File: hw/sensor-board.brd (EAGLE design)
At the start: 50 x 40 mm, 55 parts, among them U1 LT1762EMS8-3.3PBF, U2 ULN2003LVPWR, U3 ULN2003LVPWR, U4 PCA9685PW, U5 AT42QT1070-SSU, U6 TPS730XX, X1 MOLEX-501953-0407, X2 MOLEX-501953-0407

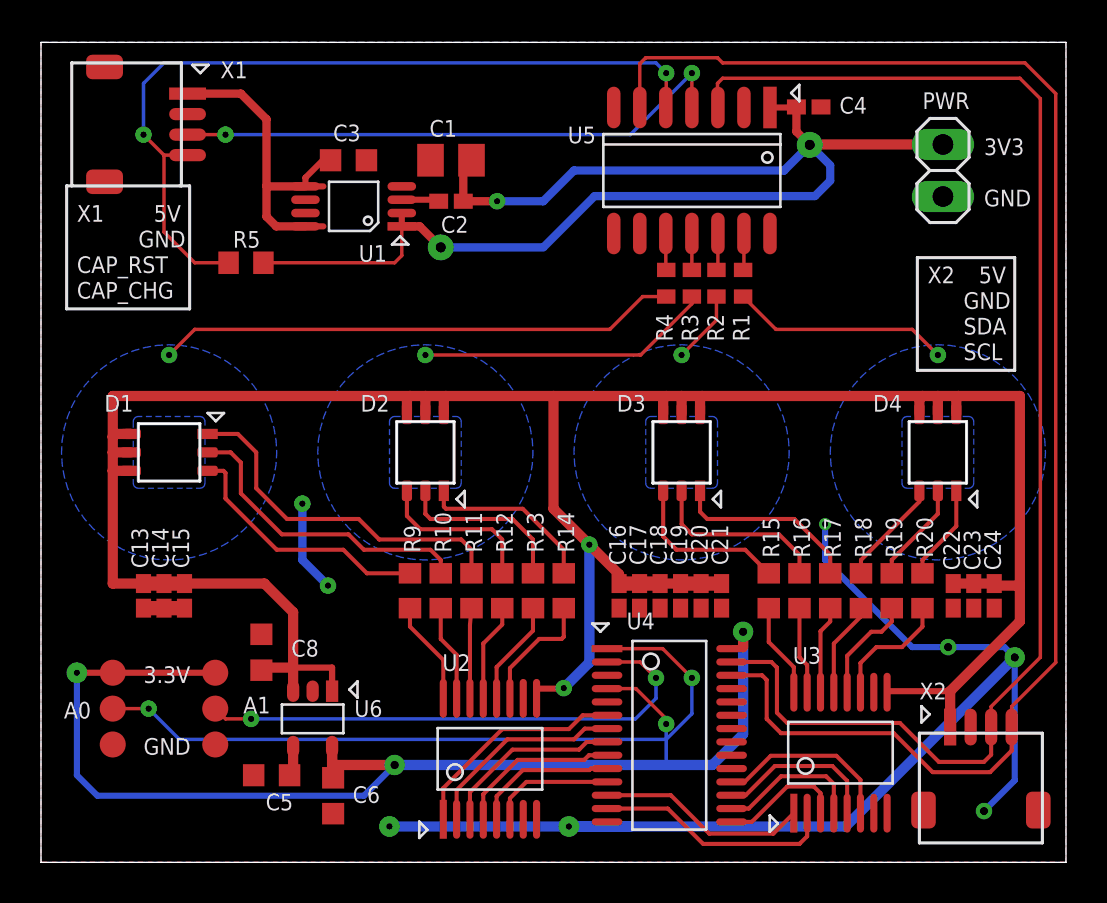
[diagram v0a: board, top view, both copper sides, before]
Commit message: Update part number and values for LDO caps.
Optimize cap placement near LDOs.
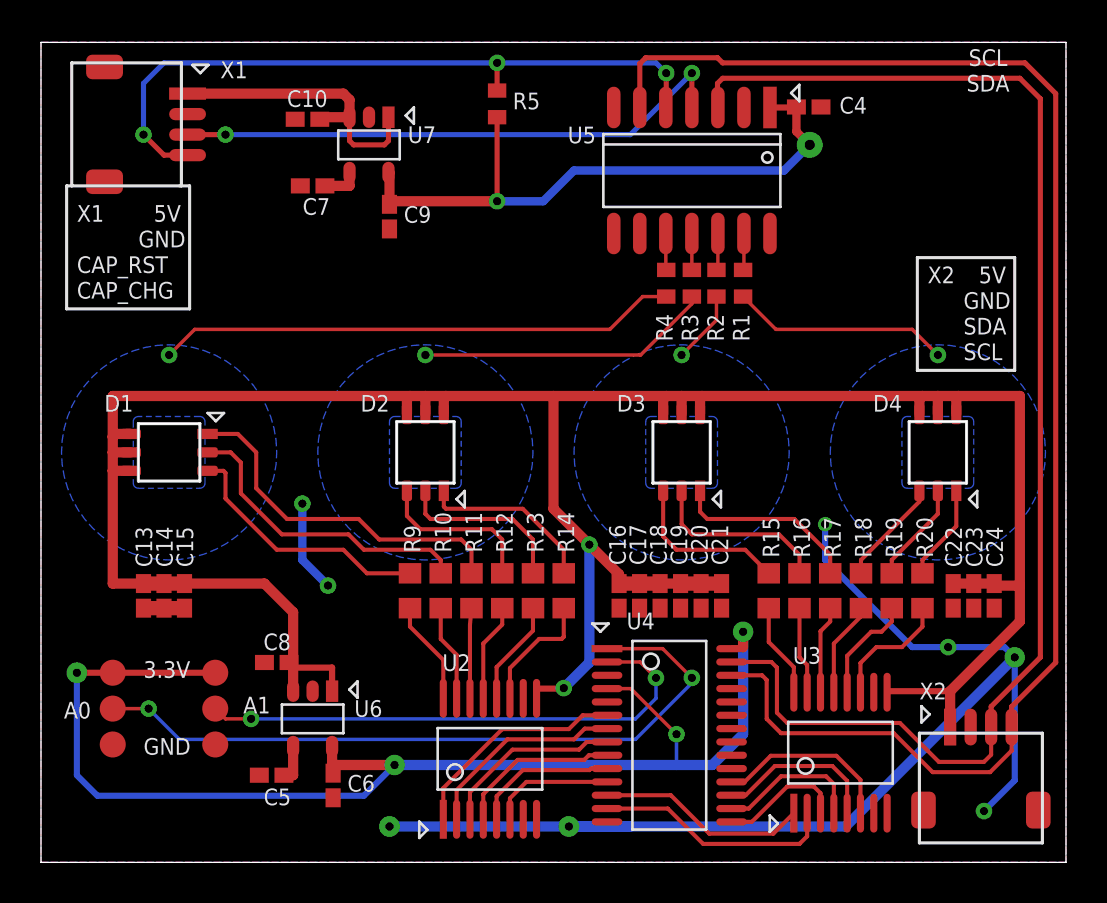
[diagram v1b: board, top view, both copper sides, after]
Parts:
- removed C1: 10uF 10V, rcl:C0805K
- removed C2: 0.01uF 25V, rcl:C0402K
- removed C3: 1uF 16V, rcl:C0603K
- removed PWR: (no value), pinhead:1X02
- removed U1: LT1762EMS8-3.3PBF, vreg:LINEAR-MS8-MSOP8
- added C10: 1uF 25V, rcl:C0402K
- added C7: 0.01uF 25V, rcl:C0402K
- added C9: 2.2uF 10V, rcl:C0402K
- added U7: TPS730XX, vreg:SOT23-5
- C5, C8: device rcl:C0603K -> rcl:C0402K
- C6: value 1uF 25V -> 2.2uF 10V; device rcl:C0603K -> rcl:C0402K
- R5: device myrcl:R0603 -> myrcl:R0402
- moved R5 14.5 mm to (22.2, 37.0), turned to 270 degrees
- moved C8 0.90 mm to (11.5, 9.75), turned to 180 degrees
- moved C6 0.50 mm to (14.2, 3.75)
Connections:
- net GND: now also C10.1, C7.2, C9.2, U7.2; no longer C1.2, C3.2, PWR.2, U1.4
- net N$8: now also C7.1, U7.4; no longer C2.1, U1.3
- net VDD_3_3: now also C9.1, U7.5; no longer C1.1, C2.2, PWR.1, U1.1, U1.2
- net VDD_5: now also C10.2, U7.1, U7.3; no longer C3.1, U1.5, U1.8
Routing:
- net VDD_3_3: track 64.2 -> 30.9 mm, vias 3 -> 2
- net !CAPSENSE_CHG!: track 40.4 -> 34.2 mm, vias 2 -> 3
- net VDD_5: track 148.1 -> 144.6 mm
- net N$9: track 65.8 -> 62.9 mm
- net N$6: track 35.9 -> 35.0 mm
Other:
- board text removed: "3V3"

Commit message: Route unused sensing lines to test points.
Resolve DRC issues due to silkscreen over stop mask.
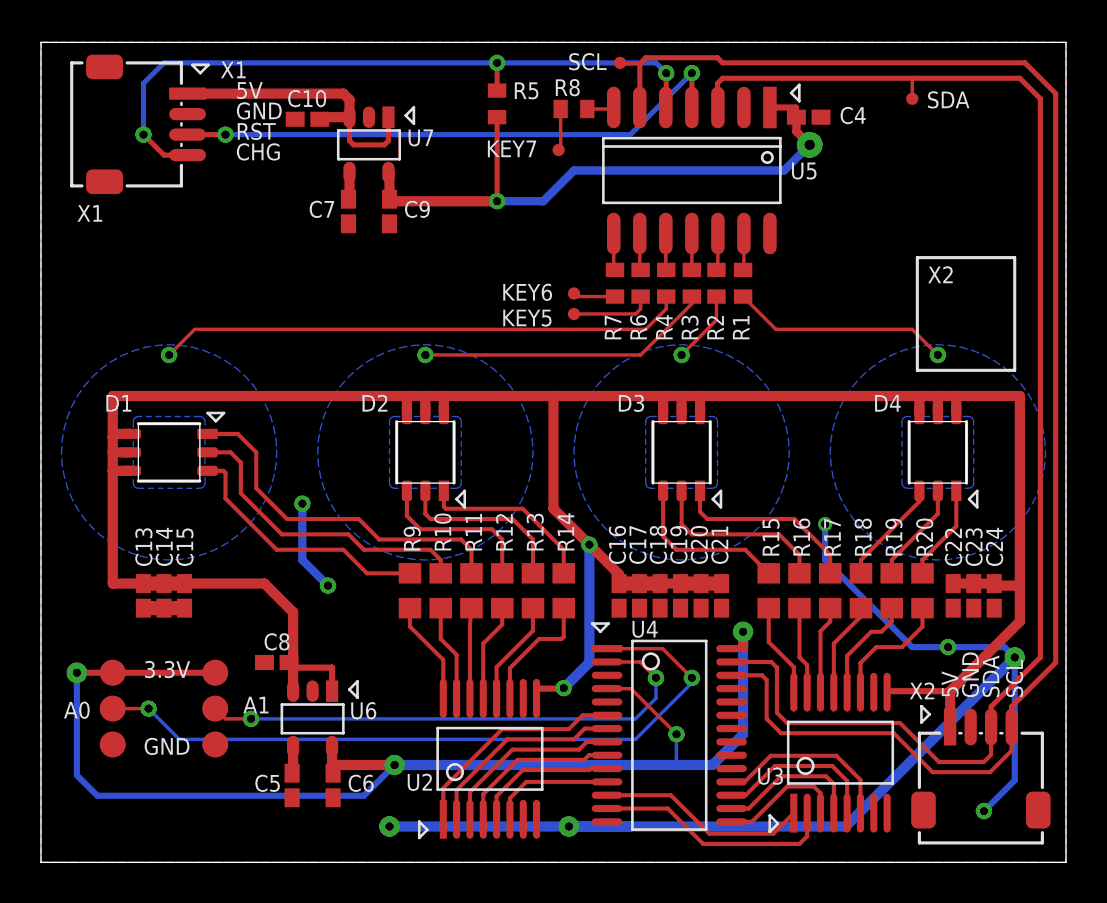
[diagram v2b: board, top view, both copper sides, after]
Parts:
- added KEY5, KEY6, KEY7, SCL, SDA: TPTP06R, testpad:TP06R
- added R6, R7, R8: 4.7k, myrcl:R0402
- moved C7 2.15 mm to (15.0, 31.8), turned to 270 degrees
- moved C5 1.12 mm to (12.2, 3.75), turned to 270 degrees
- moved C4 0.50 mm to (37.5, 36.4)
- moved C9 0.25 mm to (17.0, 31.8)
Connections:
- new net KEY5: KEY5.TP, R6.2
- new net KEY6: KEY6.TP, R7.2
- new net KEY7: KEY7.TP, R8.2
- new net N$10: R6.1, U5.9
- new net N$11: R7.1, U5.8
- new net N$12: R8.1, U5.7
- net SCL: now also SCL.TP
- net SDA: now also SDA.TP
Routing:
- net KEY5: track 0.00 -> 3.95 mm
- net KEY6: track 0.00 -> 2.06 mm
- net KEY7: track 0.00 -> 2.04 mm
- net N$11: track 0.00 -> 1.80 mm
- net N$10: track 0.00 -> 1.79 mm
- net N$12: track 0.00 -> 1.32 mm
- net SDA: track 66.6 -> 67.6 mm
- net SCL: track 73.4 -> 74.4 mm
- net N$8: track 1.85 -> 1.32 mm
- net N$1: track 1.85 -> 1.32 mm
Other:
- board text added: "CHG"
- board text added: "RST"
- board text removed: "CAP_CHG"
- board text removed: "CAP_RST"

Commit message: Sync part names for LED caps and resistors.
Label power supply nets.
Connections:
- net N$9 renamed VDD_3_3_PWMDRIVE
- net VDD_3_3 renamed VDD_3_3_CAPSENSE
- removed net VDD_5: C10.2, C13.2, C14.2, C15.2, C16.2, C17.2, C18.2, C19.2, C20.2, C21.2, C22.2, C23.2, C24.2, C8.1, D1.4, D1.5, D1.6, D2.4, D2.5, D2.6, D3.4, D3.5, D3.6, D4.4, D4.5, D4.6, U2.9, U3.9, U6.1, U6.3, U7.1, U7.3, X1.1, X2.1
- new net VDD_5_CAPSENSE: C10.2, U7.1, U7.3, X1.1
- new net VDD_5_ILLUM: C13.2, C14.2, C15.2, C16.2, C17.2, C18.2, C19.2, C20.2, C21.2, C22.2, C23.2, C24.2, C8.1, D1.4, D1.5, D1.6, D2.4, D2.5, D2.6, D3.4, D3.5, D3.6, D4.4, D4.5, D4.6, U2.9, U3.9, U6.1, U6.3, X2.1
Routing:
- net VDD_5: track 144.6 -> 0.00 mm, vias 2 -> 0
- net VDD_5_ILLUM: track 0.00 -> 129.9 mm, vias 0 -> 2
- net VDD_5_CAPSENSE: track 0.00 -> 14.7 mm
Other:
- board text removed: "X2"

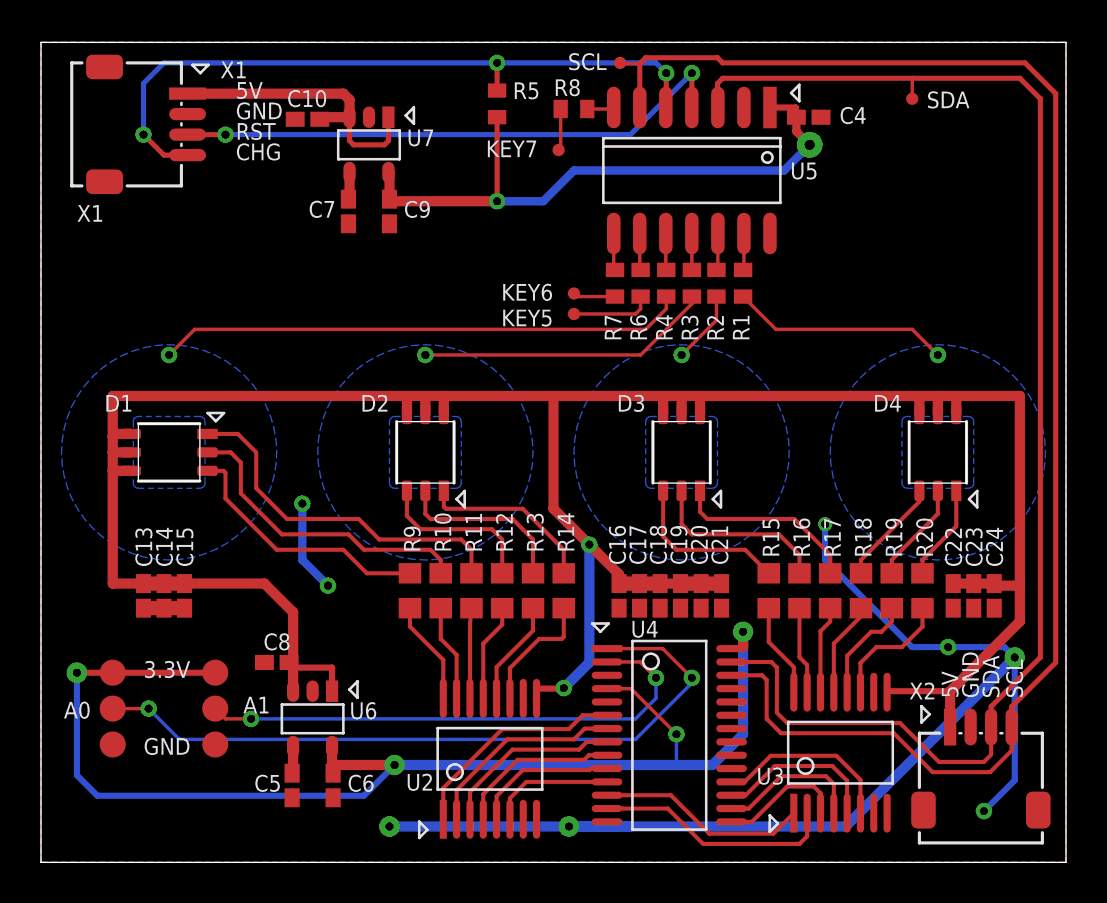
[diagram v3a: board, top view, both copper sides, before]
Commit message: Reduce fpanel PCB height to 39mm.
This reduction in height will help fit the pcb into standard 5.25" bays.
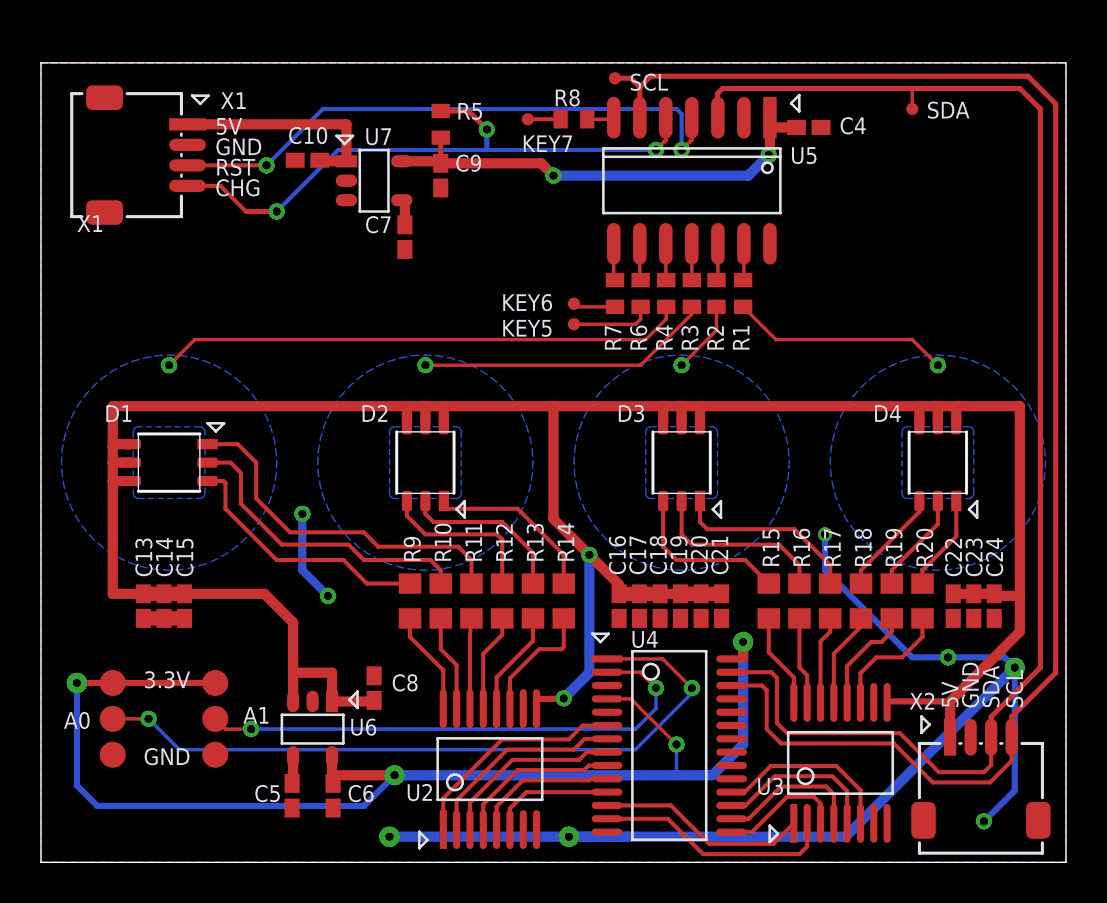
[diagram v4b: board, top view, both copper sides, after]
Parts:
- moved C8 4.91 mm to (16.2, 8.50), turned to 90 degrees
- moved C9 3.05 mm to (19.5, 33.5)
- moved C7 3.02 mm to (17.8, 30.5)
- moved R5 2.93 mm to (19.5, 36.0)
- moved KEY7 2.12 mm to (23.8, 36.2), turned to 270 degrees
- moved C10 2.00 mm to (13.0, 34.2)
- moved U7 1.77 mm to (16.2, 33.2), turned to 270 degrees
- moved X1 1.50 mm to (1.50, 34.5)
- moved SCL 0.79 mm to (28.0, 38.2)
- moved 3.3V 0.50 mm to (8.50, 8.75)
- moved A0 0.50 mm to (3.50, 7.00)
- moved A1 0.50 mm to (8.50, 7.00)
- moved C13 0.50 mm to (5.00, 12.5)
- moved C14 0.50 mm to (6.00, 12.5)
- moved C15 0.50 mm to (7.00, 12.5)
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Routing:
- net VDD_3_3_CAPSENSE: track 30.6 -> 23.5 mm
- net !CAPSENSE_CHG!: track 34.2 -> 30.0 mm
- net VDD_5_CAPSENSE: track 14.7 -> 10.9 mm
- net VDD_5_ILLUM: track 129.9 -> 131.9 mm
- net !CAPSENSE_RST!: track 27.5 -> 28.9 mm
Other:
- board size 50 x 40 mm -> 50 x 39 mm

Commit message: Move SCL and SDA lines closer to inside.
This is done to improve manufacturing reliability.
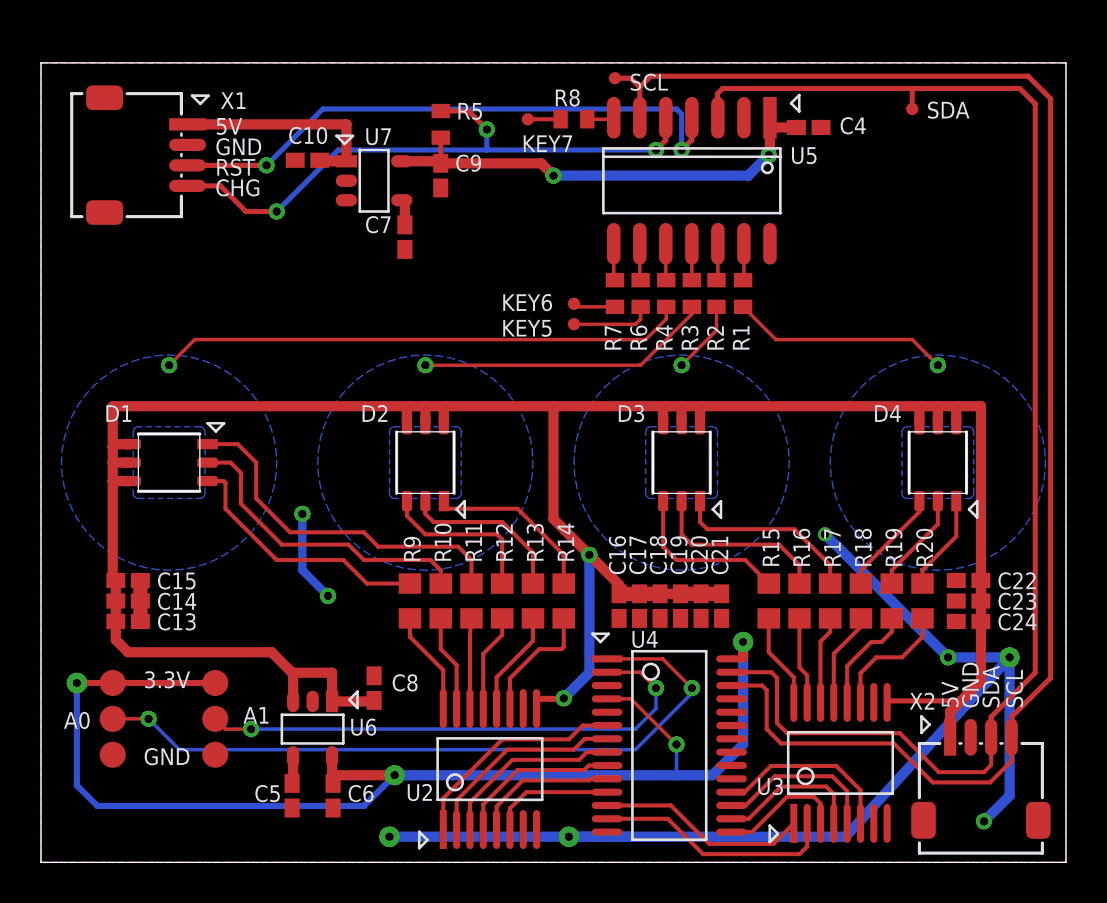
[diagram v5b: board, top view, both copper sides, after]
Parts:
- moved C15 3.02 mm to (4.25, 13.8), turned to 180 degrees
- moved C14 1.77 mm to (4.25, 12.8), turned to 180 degrees
- moved C22 1.46 mm to (45.2, 13.8), turned to 0 degrees
- moved C24 1.46 mm to (45.2, 11.8), turned to 0 degrees
- moved C13 1.06 mm to (4.25, 11.8), turned to 180 degrees
- moved C23 0.35 mm to (45.2, 12.8), turned to 0 degrees
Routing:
- net VDD_5_ILLUM: track 131.9 -> 126.6 mm
- net GND: track 64.5 -> 63.6 mm
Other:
- board text removed: "X1"
